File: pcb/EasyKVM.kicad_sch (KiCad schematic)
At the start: 25 parts, among them J1 USB_A, J4 USB_B_Micro, J5 USB_B_Micro, J6 HDMI_A, J8 HDMI_A, J9 USB_A, Q3 BSS138, Q4 BSS138, U1 SP0503BAHT, U2 LM3525M-H, U3 SP0503BAHT, U4 MAX4999ETJ+, U7 SP0503BAHT

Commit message: routing start
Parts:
- added R2, R3: 100K, Resistor_SMD:R_0603_1608Metric, symbol Device:R
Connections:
- net ESD_PC1_USB_N: now also D5.2 (K); no longer D5.1 (K)
- net ESD_PC1_USB_P: now also D5.1 (K); no longer D5.2 (K)
- net ESD_PC2_USB_N: now also D6.2 (K); no longer D6.1 (K)
- net ESD_PC2_USB_P: now also D6.1 (K); no longer D6.2 (K)
- net GND: now also R2.1, R3.2
- net HUB_USB_N: now also U3.4 (K); no longer U3.3 (K)
- net HUB_USB_P: now also U3.3 (K); no longer U3.4 (K)
- net KVM_ENABLE: now also R2.2; no longer U2.1 (EN)
- net OVER_CURRENT: now reaches U2.2 (FLAG)
- new net USB_ENABLE: R3.1, U2.1 (EN)
- no-connect marks 20 -> 19
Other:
- moved on the sheet: C3, C4, J4, J5, U4

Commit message: design bugs case update software bugs
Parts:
- removed D4, D5, D6: SP0502BAHT, Package_TO_SOT_SMD:SOT-23, symbol Power_Protection:SP0502BAHT
- removed U1, U3, U7: SP0503BAHT, Package_TO_SOT_SMD:SOT-143, symbol Power_Protection:SP0503BAHT
- added U1, U11, U4, U5, U8, U9: SP3003-02XTG, Package_TO_SOT_SMD:Diodes_SOT-553, symbol MyParts:SP3003-02XTG
- renumbered C21 to C11, C1 to C13, C2 to C15, C4 to C5, C3 to C6, J4 to J1, J5 to J2, J8 to J3, J6 to J5, J9 to J6, J1 to J7, Q4 to Q2, R2 to R1, R27 to R12, R28 to R17, R3 to R2, R33 to R6, R26 to R7, U2 to U10, U4 to U6
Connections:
- net 3.3V: now also C5.1, C6.2, U6.2 (VCC_1), U6.20 (VCC_2)
- net ESD_DDC_SCL: now also U5.4 (IO2)
- net ESD_DDC_SDA: now also U5.5 (IO1)
- net ESD_PC1_USB_N: now also U4.4 (IO2)
- net ESD_PC1_USB_P: now also U4.5 (IO1)
- net ESD_PC2_USB_N: now also U1.4 (IO2)
- net ESD_PC2_USB_P: now also U1.5 (IO1)
- net ESD_USB_N: now also U8.4 (IO2)
- net ESD_USB_P: now also U8.5 (IO1)
- net ESD_VBUS: now also U8.3 (VCC)
- net GND: now also J7.5 (Shield), U1.2 (GND), U11.2 (GND), U4.2 (GND), U5.2 (GND), U8.2 (GND), U9.2 (GND)
- net HDMI_5V: now also U5.3 (VCC)
- net HUB_USB_N: now also U11.4 (IO2)
- net HUB_USB_P: now also U11.5 (IO1)
- net HUB_VBUS: now also U11.3 (VCC)
- net KBD_USB_N: now also U9.4 (IO2)
- net KBD_USB_P: now also U9.5 (IO1)
- net VBUS: now also U9.3 (VCC)
- no-connect marks 19 -> 26

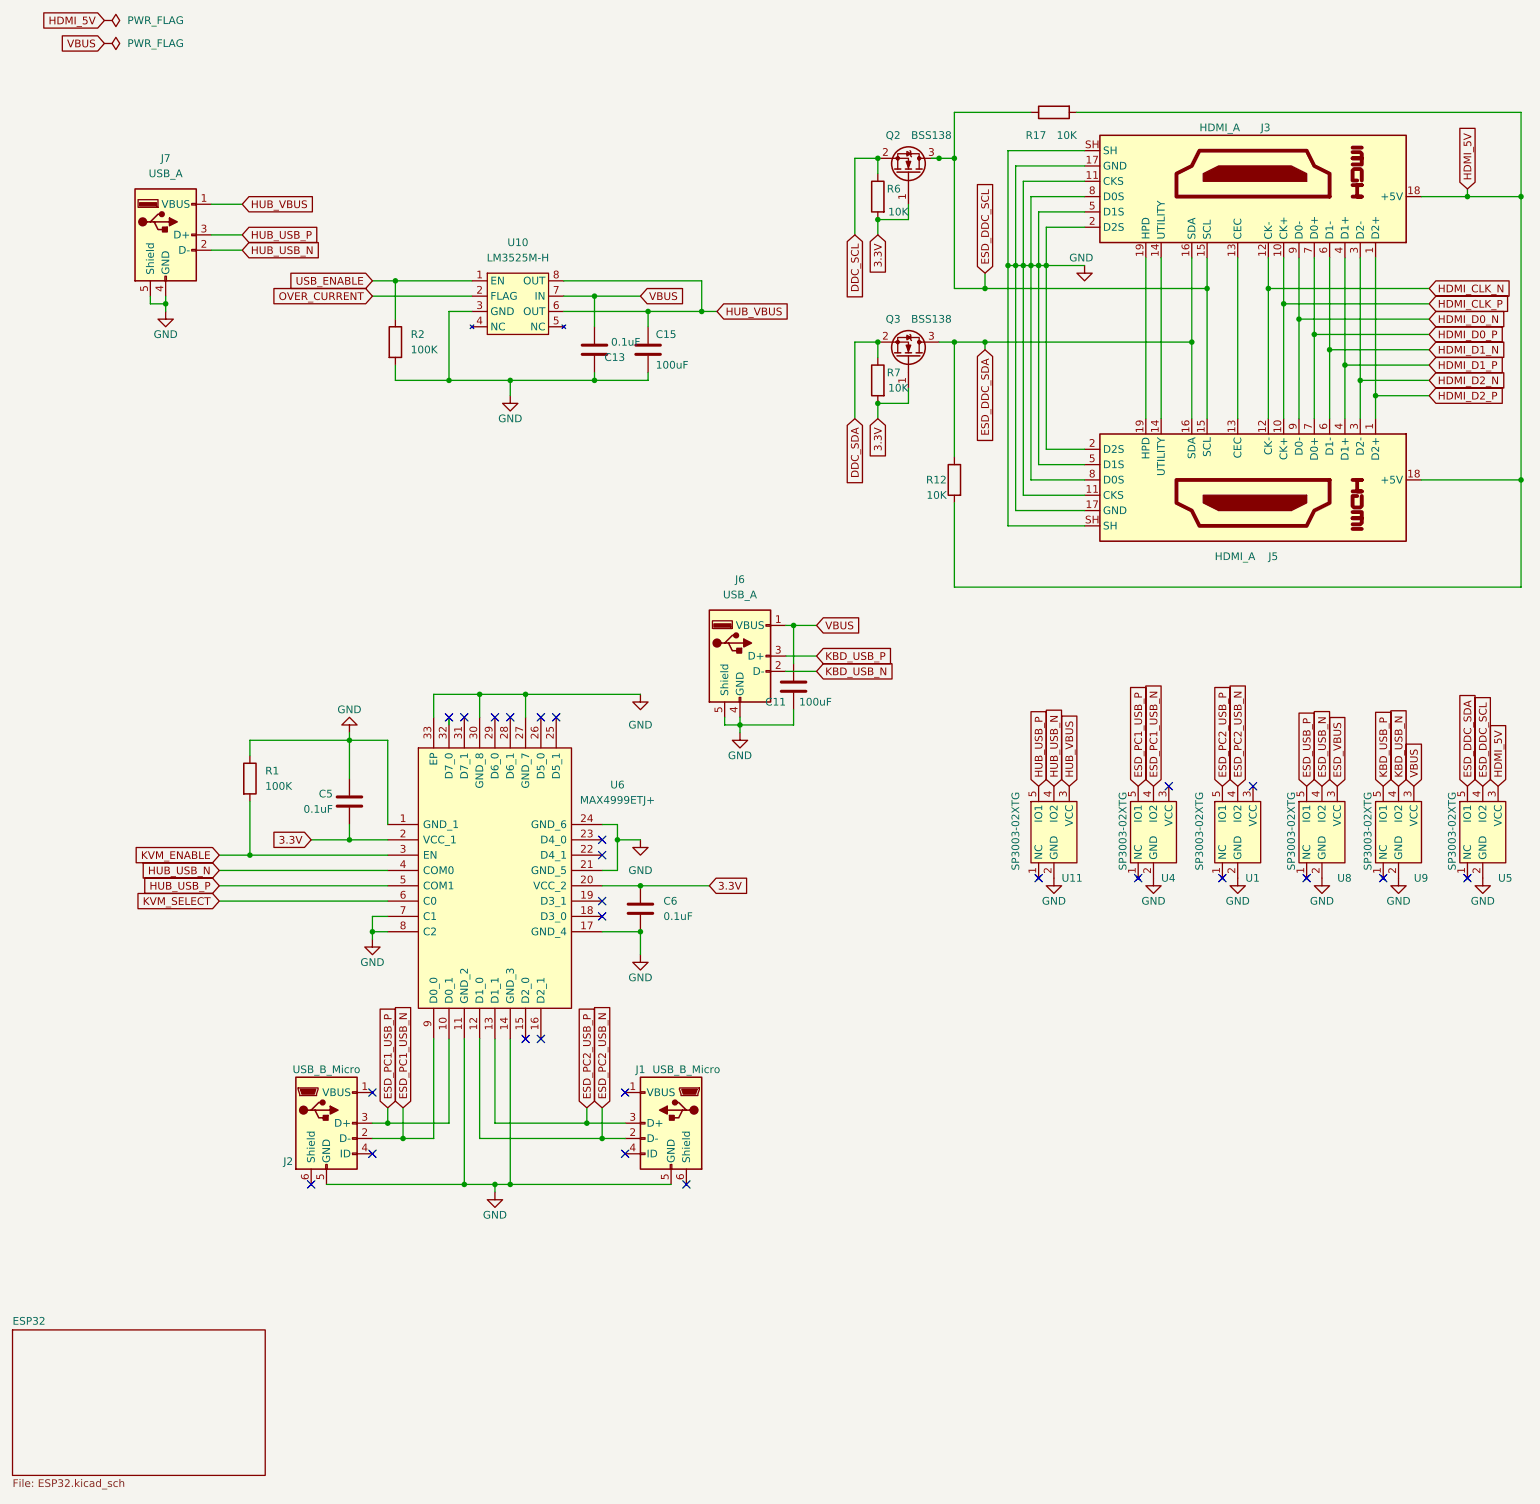
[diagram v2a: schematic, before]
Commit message: Fix cornerns Add hub diode R3
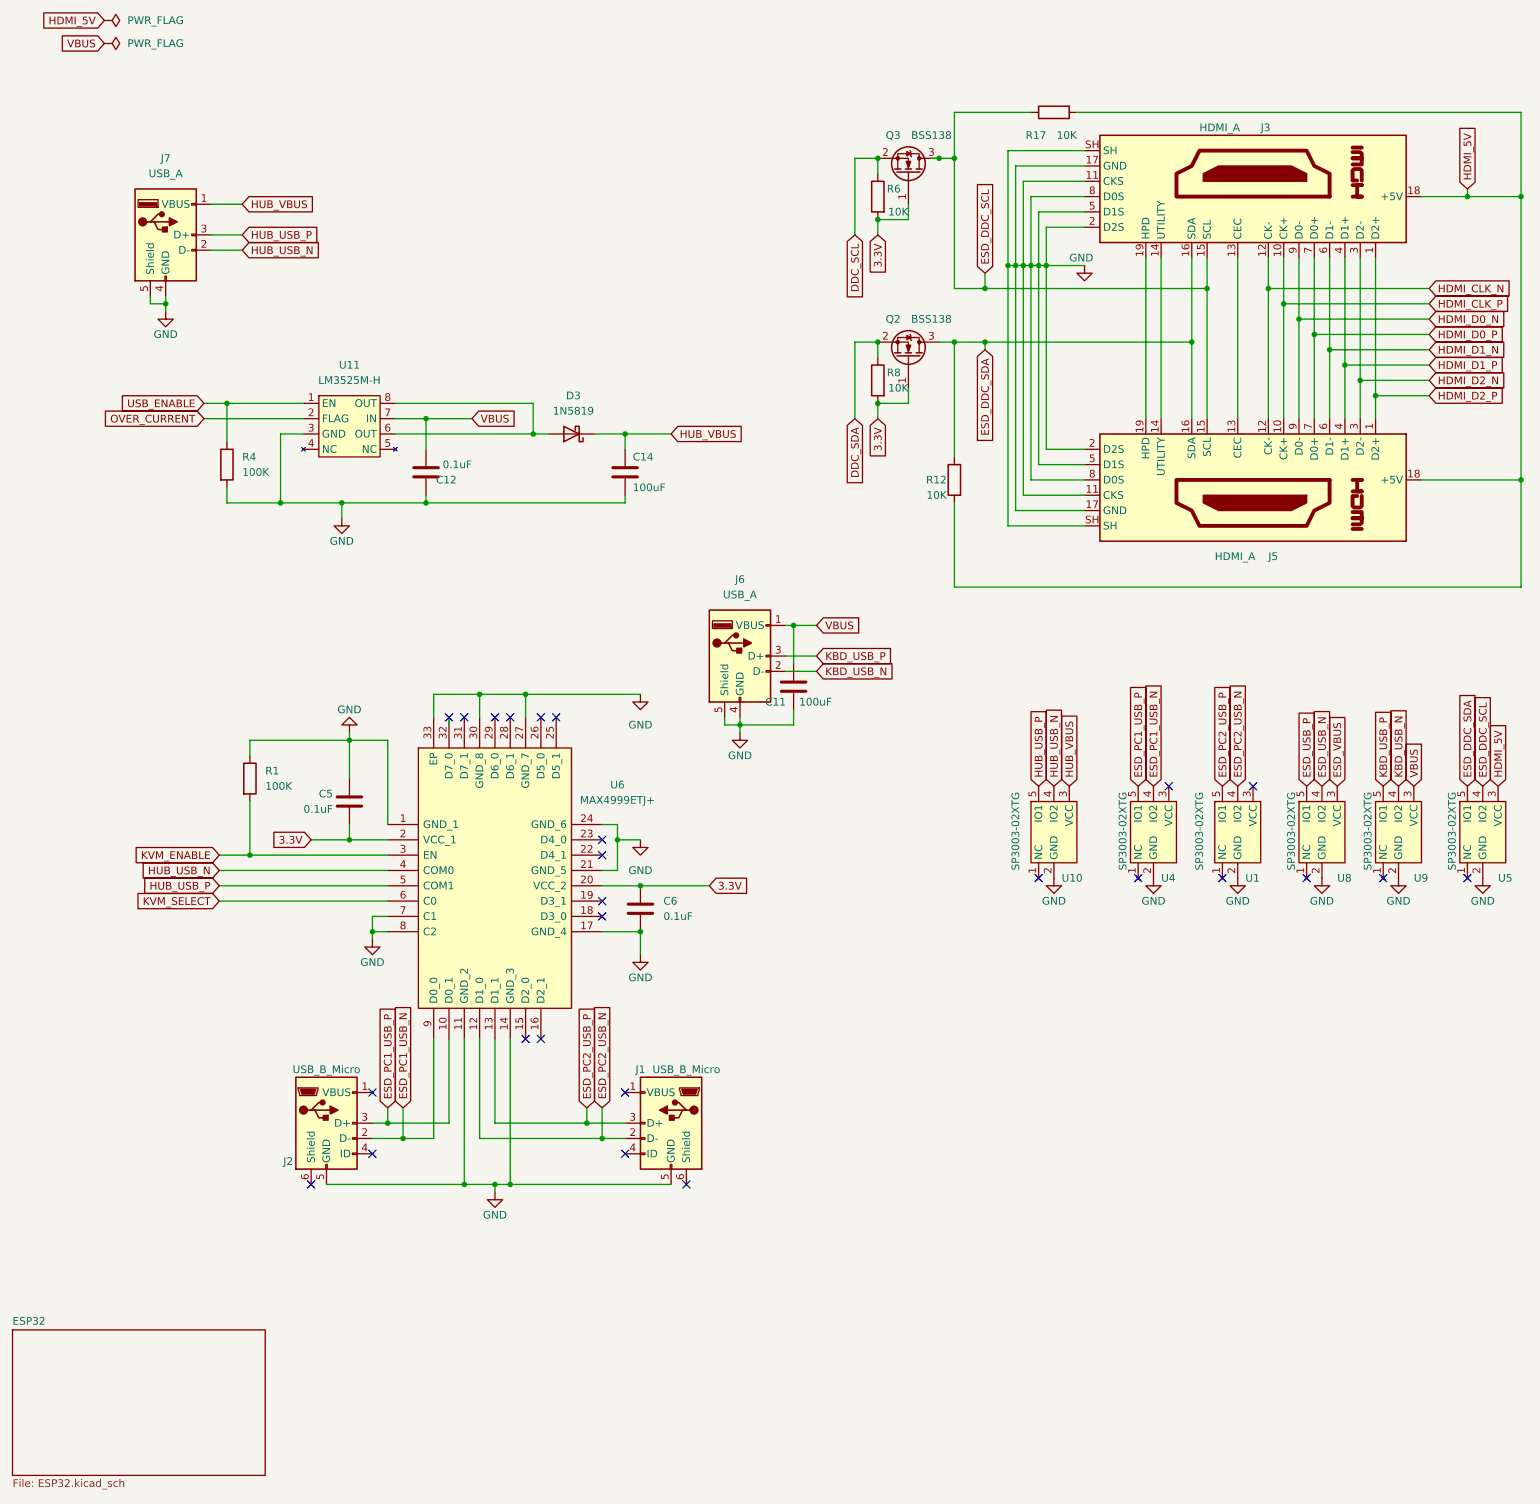
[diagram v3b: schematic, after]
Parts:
- added D3: 1N5819, Diode_SMD:D_SOD-323, symbol Diode:1N5819
- renumbered C13 to C12, C15 to C14, Q3 to Q2, Q2 to Q3, R2 to R4, R7 to R8, U11 to U10, U10 to U11
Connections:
- net HUB_VBUS: now also D3.1 (K); no longer U11.6 (OUT), U11.8 (OUT)
- new net: D3.2 (A), U11.6 (OUT), U11.8 (OUT)
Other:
- moved on the sheet: C12, C14, R4, U11

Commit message: usb resets lower ble advertising reorder references
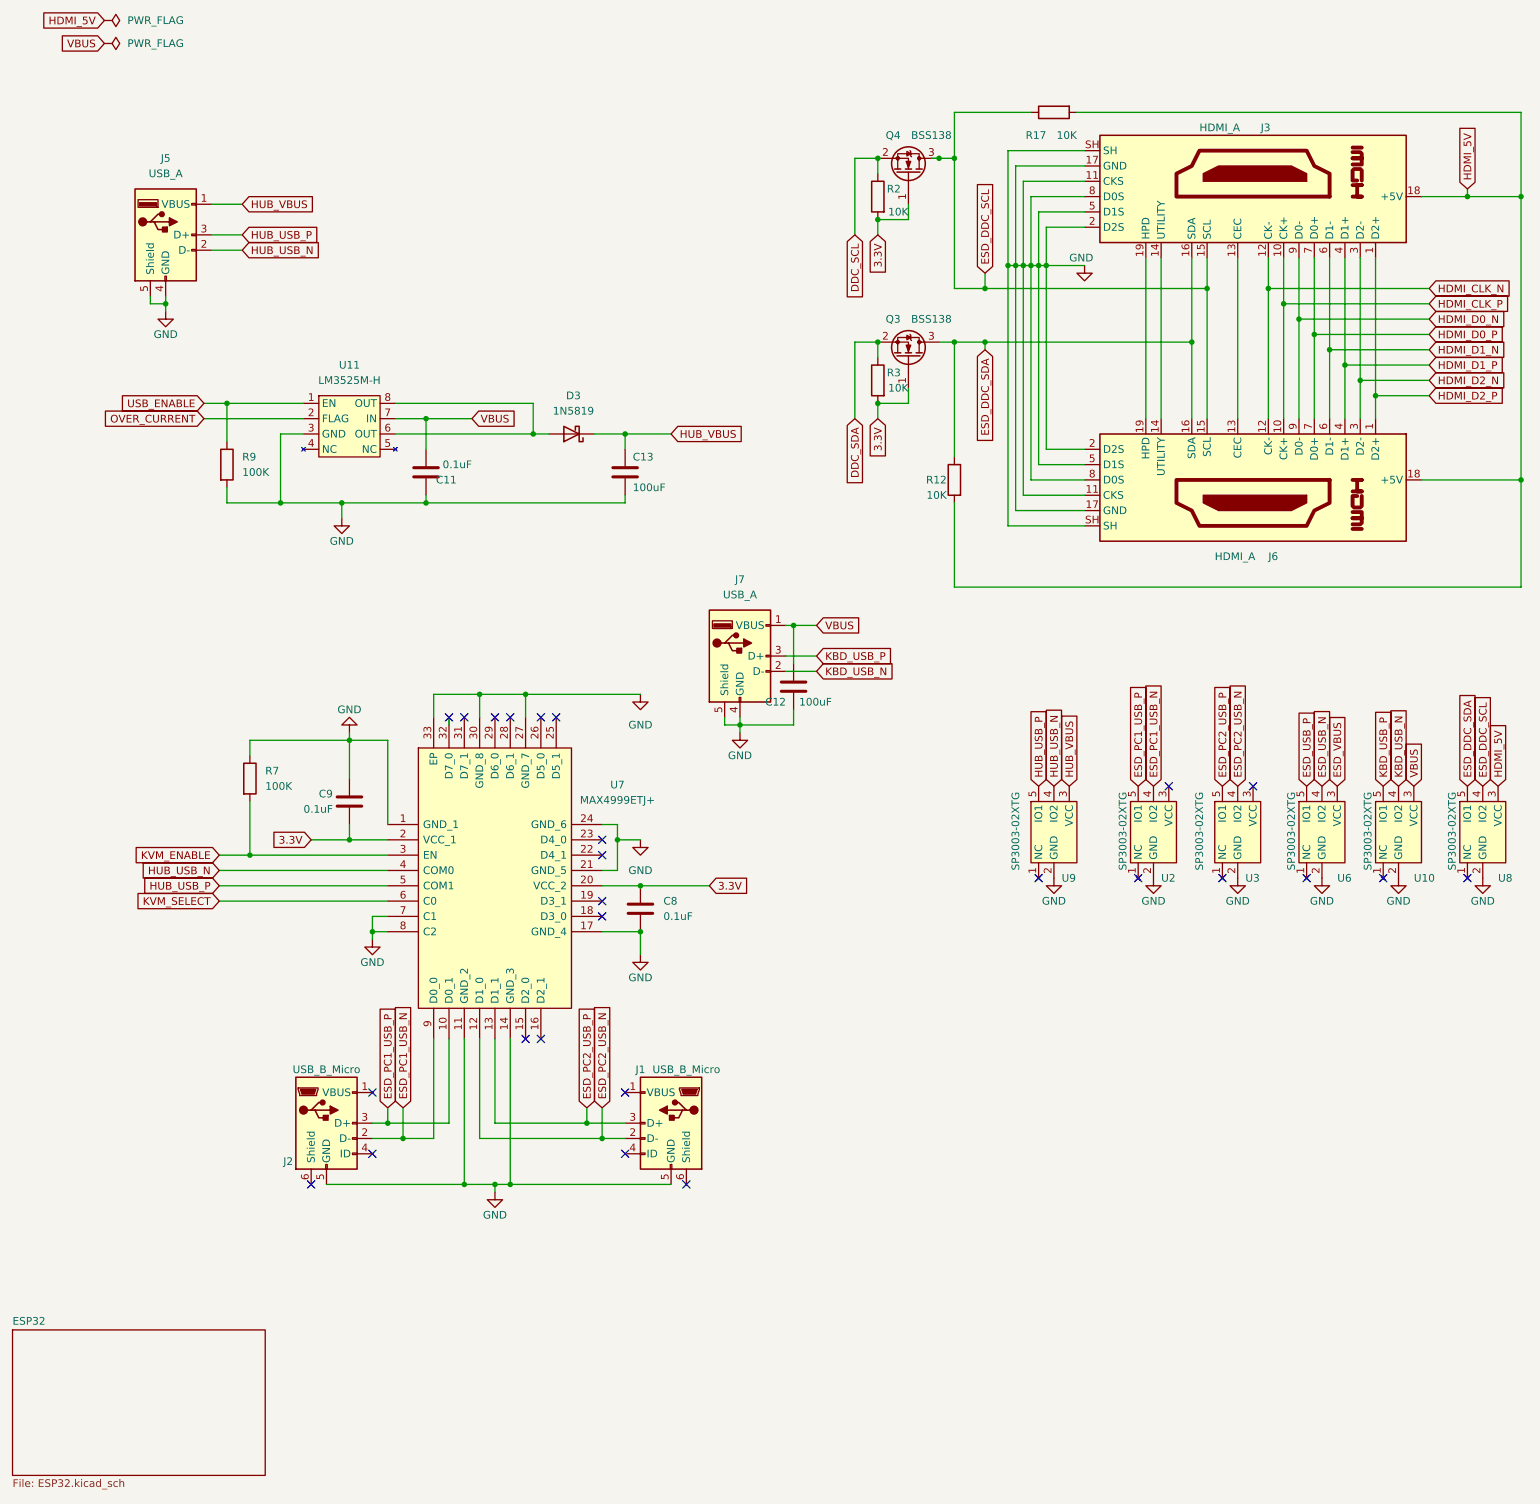
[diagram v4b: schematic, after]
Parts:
- renumbered C12 to C11, C11 to C12, C14 to C13, C6 to C8, C5 to C9, J7 to J5, J5 to J6, J6 to J7, Q2 to Q3, Q3 to Q4, R6 to R2, R8 to R3, R1 to R7, R4 to R9, U9 to U10, U4 to U2, U1 to U3, U8 to U6, U6 to U7, U5 to U8, U10 to U9
